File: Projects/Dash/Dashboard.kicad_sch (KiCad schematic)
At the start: 0 parts

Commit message: [2026-09-18] First commit to dash branch
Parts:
- added A1: Arduino_Nano_Socket, Arduino Nano:Arduino_Nano_Socket, symbol arduino-library:Arduino_Nano_Socket
- added J1: Conn_01x02_Pin, Connector:Tag-Connect_TC2030-IDC-FP_2x03_P1.27mm_Vertical, symbol Connector:Conn_01x02_Pin
- added U2: Adafruit-CAN-BFF-SMD, Adafruit_CAN_BFF:Adafruit-CAN-BFF-SMD, symbol Adafruit_CAN_BFF:Adafruit-CAN-BFF-SMD
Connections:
- new net +5V: A1.5V, J1.1 (Pin_1), U2.14 (5V)
- new net CAN_CS: U2.4 (CS/A3/D3)
- new net CAN_INT: U2.1 (INT/A0/D0)
- new net GND: A1.GND1 (GND), J1.2 (Pin_2), U2.13 (GND)
- new net I2C_SCL: A1.A5 (A5/SCL)
- new net I2C_SDA: A1.A4 (A4/SDA)
- new net SERVO_SPEED: A1.D6
- new net SERVO_TACH: A1.D5
- new net SPI_SCK: U2.9 (SCK/D8)
- new net SPI_SI: U2.11 (MOSI/D10)
- new net SPI_SO: U2.10 (MISO/D9)
- no-connect marks 0 -> 31

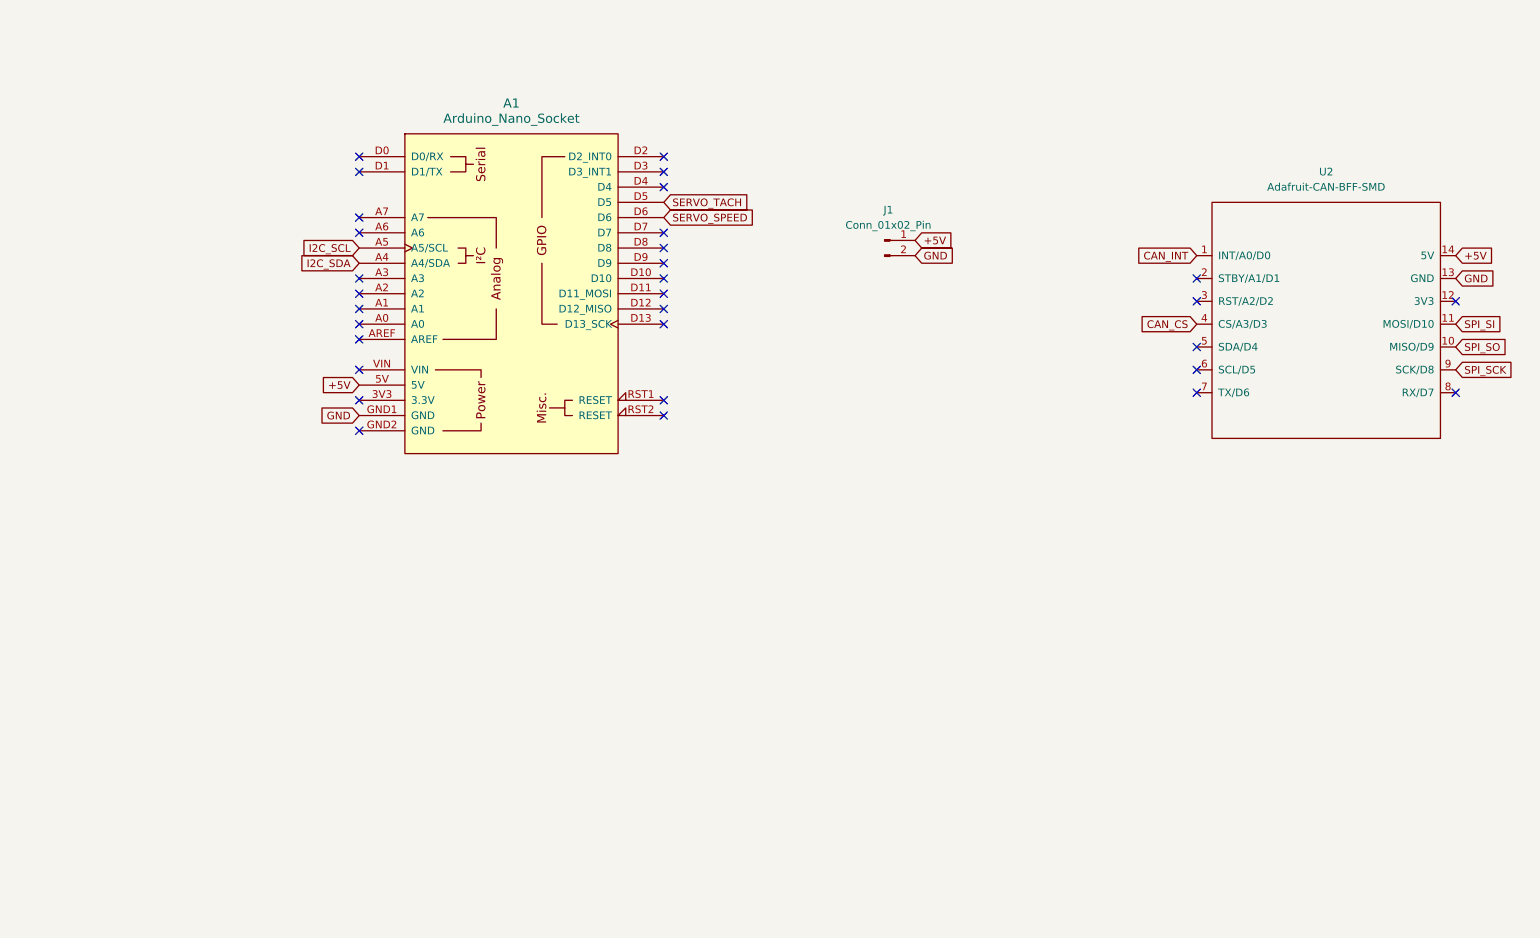
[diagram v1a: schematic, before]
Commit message: [2026-09-18] Further schematic and PCB setup
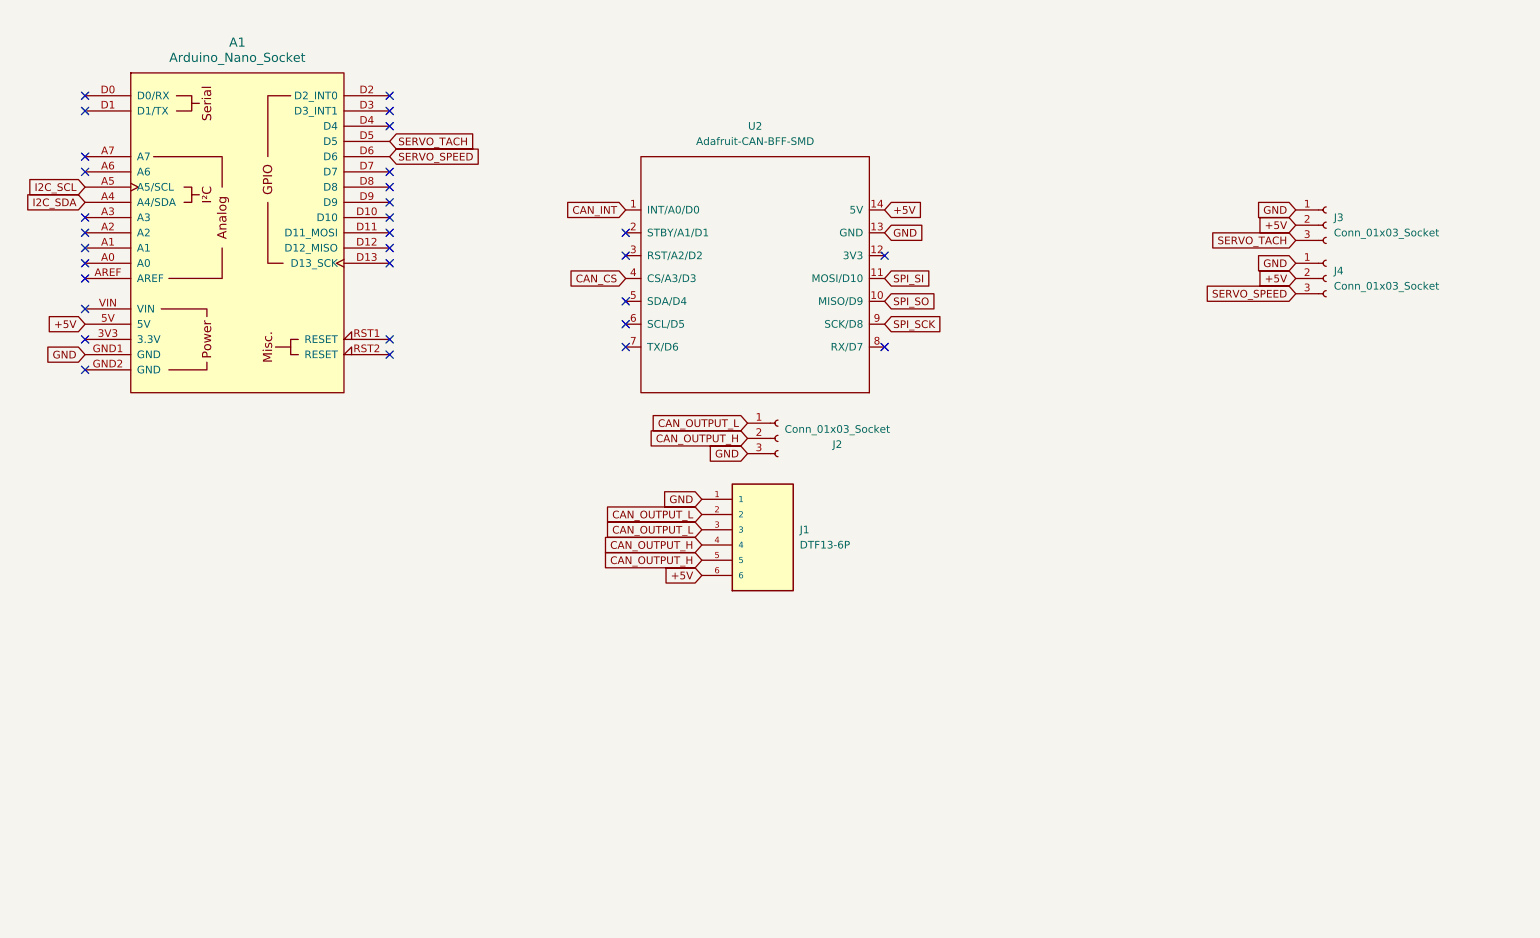
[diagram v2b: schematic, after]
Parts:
- removed J1: Conn_01x02_Pin, Connector:Tag-Connect_TC2030-IDC-FP_2x03_P1.27mm_Vertical, symbol Connector:Conn_01x02_Pin
- added J1: DTF13-6P, DTF13-6P:TE_DTF13-6P, symbol DTF13-6P:DTF13-6P
- added J2, J3, J4: Conn_01x03_Socket, symbol Connector:Conn_01x03_Socket
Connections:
- net +5V: now also J1.6, J3.2 (Pin_2), J4.2 (Pin_2)
- net GND: now also J1.1, J2.3 (Pin_3), J3.1 (Pin_1), J4.1 (Pin_1)
- net SERVO_SPEED: now also J4.3 (Pin_3)
- net SERVO_TACH: now also J3.3 (Pin_3)
- new net CAN_OUTPUT_H: J1.4, J1.5, J2.2 (Pin_2)
- new net CAN_OUTPUT_L: J1.2, J1.3, J2.1 (Pin_1)
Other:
- moved on the sheet: A1, U2

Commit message: [2026-09-19] Dash REV 1 Done
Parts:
- added J10: R2C3 (0x75), Connector_PinHeader_2.54mm:PinHeader_1x05_P2.54mm_Vertical, symbol Connector:Conn_01x05_Pin
- added J11: Top Row Button, Connector_PinHeader_2.54mm:PinHeader_1x02_P2.54mm_Vertical, symbol Connector:Conn_01x02_Pin
- added J12: Bottom Row Button, Connector_PinHeader_2.54mm:PinHeader_1x02_P2.54mm_Vertical, symbol Connector:Conn_01x02_Pin
- added J5: R1C1 (0x70), Connector_PinHeader_2.54mm:PinHeader_1x05_P2.54mm_Vertical, symbol Connector:Conn_01x05_Pin
- added J6: R1C2 (0x71), Connector_PinHeader_2.54mm:PinHeader_1x05_P2.54mm_Vertical, symbol Connector:Conn_01x05_Pin
- added J7: R1C3 (0x72), Connector_PinHeader_2.54mm:PinHeader_1x05_P2.54mm_Vertical, symbol Connector:Conn_01x05_Pin
- added J8: R2C1 (0x73), Connector_PinHeader_2.54mm:PinHeader_1x05_P2.54mm_Vertical, symbol Connector:Conn_01x05_Pin
- added J9: R2C2 (0x74), Connector_PinHeader_2.54mm:PinHeader_1x05_P2.54mm_Vertical, symbol Connector:Conn_01x05_Pin
- J1: value DTF13-6P -> Deutsch Connector
- J2: value Conn_01x03_Socket -> CAN BFF Intercepting Header; footprint (none) -> Connector_PinHeader_2.54mm:PinHeader_1x03_P2.54mm_Vertical
- J3: value Conn_01x03_Socket -> Tach Servo Header; footprint (none) -> Connector_PinHeader_2.54mm:PinHeader_1x03_P2.54mm_Vertical
- J4: value Conn_01x03_Socket -> Speed Servo Header; footprint (none) -> Connector_PinHeader_2.54mm:PinHeader_1x03_P2.54mm_Vertical
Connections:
- net +5V: now also J10.1 (Pin_1), J10.2 (Pin_2), J5.1 (Pin_1), J5.2 (Pin_2), J6.1 (Pin_1), J6.2 (Pin_2), J7.1 (Pin_1), J7.2 (Pin_2), J8.1 (Pin_1), J8.2 (Pin_2), J9.1 (Pin_1), J9.2 (Pin_2)
- net GND: now also J10.3 (Pin_3), J11.1 (Pin_1), J12.1 (Pin_1), J5.3 (Pin_3), J6.3 (Pin_3), J7.3 (Pin_3), J8.3 (Pin_3), J9.3 (Pin_3)
- net I2C_SCL: now also J10.5 (Pin_5), J5.5 (Pin_5), J6.5 (Pin_5), J7.5 (Pin_5), J8.5 (Pin_5), J9.5 (Pin_5)
- net I2C_SDA: now also J10.4 (Pin_4), J5.4 (Pin_4), J6.4 (Pin_4), J7.4 (Pin_4), J8.4 (Pin_4), J9.4 (Pin_4)
- net SERVO_SPEED: now also A1.D9; no longer A1.D6
- net SERVO_TACH: now also A1.D10; no longer A1.D5
- net BUTTON_TOP: now reaches A1.D7
- net BUTTON_TOP: now also J11.2 (Pin_2)
- net BUTTON_BOTTOM: now reaches A1.D8
- net BUTTON_BOTTOM: now also J12.2 (Pin_2)
- no-connect marks 31 -> 29
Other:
- moved on the sheet: J1, J2, J3, J4, U2

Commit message: Guess who forgot the SPI bus 😂
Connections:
- net CAN_CS: now also A1.D6
- net CAN_INT: now also A1.D5
- net GND: now also A1.GND2 (GND)
- net SPI_SCK: now also A1.D13 (D13_SCK)
- net SPI_SI: now also A1.D11 (D11_MOSI)
- net SPI_SO: now also A1.D12 (D12_MISO)
- no-connect marks 29 -> 23
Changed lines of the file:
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@@
-	)
-	(no_connect
-		(at 81.28 62.23)
-	)
-	(no_connect
-		(at 81.28 67.31)
 	)
 	(no_connect
@@
 	)
 	(no_connect
-		(at 81.28 49.53)
-	)
-	(no_connect
-		(at 81.28 64.77)
-	)
-	(no_connect
 		(at 30.48 39.37)
 	)
@@
 	)
 	(no_connect
-		(at 81.28 46.99)
-	)
-	(no_connect
 		(at 120.65 68.58)
 	)
@@
 	)
 	(no_connect
-		(at 30.48 85.09)
-	)
-	(no_connect
 		(at 30.48 59.69)
 	)
@@
 	(global_label "GND"
 		(shape input)
+		(at 30.48 85.09 180)
+		(fields_autoplaced yes)
+		(effects
+			(font
+				(size 1.27 1.27)
+			)
+			(justify right)
+		)
+		(property "Intersheetrefs" "${INTERSHEET_REFS}"
+			(at 23.6243 85.09 0)
+			(hide yes)
+			(show_name no)
+			(do_not_autoplace no)
+			(effects
+				(font
+					(size 1.27 1.27)
+				)
+				(justify right)
+			)
+		)
+	)
+	(global_label "GND"
+		(shape input)
 		(at 30.48 82.55 180)
 		(fields_autoplaced yes)
@@
 		)
 	)
+	(global_label "SPI_SCK"
+		(shape input)
+		(at 81.28 67.31 0)
+		(fields_autoplaced yes)
+		(effects
+			(font
+				(size 1.27 1.27)
+			)
+			(justify left)
+		)
+		(property "Intersheetrefs" "${INTERSHEET_REFS}"
+			(at 92.0666 67.31 0)
+			(hide yes)
+			(show_name no)
+			(do_not_autoplace no)
+			(effects
+				(font
+					(size 1.27 1.27)
+				)
+				(justify left)
+			)
+		)
+	)
 	(global_label "GND"
 		(shape input)
@@
 		)
 	)
+	(global_label "CAN_INT"
+		(shape input)
+		(at 81.28 46.99 0)
+		(fields_autoplaced yes)
+		(effects
+			(font
+				(size 1.27 1.27)
+			)
+			(justify left)
+		)
+		(property "Intersheetrefs" "${INTERSHEET_REFS}"
+			(at 91.8248 46.99 0)
+			(hide yes)
+			(show_name no)
+			(do_not_autoplace no)
+			(effects
+				(font
+					(size 1.27 1.27)
+				)
+				(justify left)
+			)
+		)
+	)
 	(global_label "I2C_SCL"
 		(shape input)
@@
 		)
 	)
+	(global_label "SPI_SI"
+		(shape input)
+		(at 81.28 62.23 0)
+		(fields_autoplaced yes)
+		(effects
+			(font
+				(size 1.27 1.27)
+			)
+			(justify left)
+		)
+		(property "Intersheetrefs" "${INTERSHEET_REFS}"
+			(at 90.1314 62.23 0)
+			(hide yes)
+			(show_name no)
+			(do_not_autoplace no)
+			(effects
+				(font
+					(size 1.27 1.27)
+				)
+				(justify left)
+			)
+		)
+	)
 	(global_label "SERVO_TACH"
 		(shape input)
@@
 		)
 	)
+	(global_label "CAN_CS"
+		(shape input)
+		(at 81.28 49.53 0)
+		(fields_autoplaced yes)
+		(effects
+			(font
+				(size 1.27 1.27)
+			)
+			(justify left)
+		)
+		(property "Intersheetrefs" "${INTERSHEET_REFS}"
+			(at 91.4014 49.53 0)
+			(hide yes)
+			(show_name no)
+			(do_not_autoplace no)
+			(effects
+				(font
+					(size 1.27 1.27)
+				)
+				(justify left)
+			)
+		)
+	)
 	(global_label "+5V"
 		(shape input)
@@
 			)
 		)
+	)
+	(global_label "SPI_SO"
+		(shape input)
+		(at 81.28 64.77 0)
+		(fields_autoplaced yes)
+		(effects
+			(font
+				(size 1.27 1.27)
+			)
+			(justify left)
+		)
+		(property "Intersheetrefs" "${INTERSHEET_REFS}"
+			(at 90.8571 64.77 0)
+			(hide yes)
+			(show_name no)
+			(do_not_autoplace no)
+			(effects
+				(font
+					(size 1.27 1.27)
+				)
+				(justify left)
+			)
+		)
